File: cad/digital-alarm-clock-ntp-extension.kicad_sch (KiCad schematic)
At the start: 16 parts, among them J1 DigitalClock, J2 Power, J3 M5ATOM Left side, J4 M5ATOM Right side, Q1 2SC1815, Q2 2SC1815, Q3 2SC1815, Q4 2SC1815

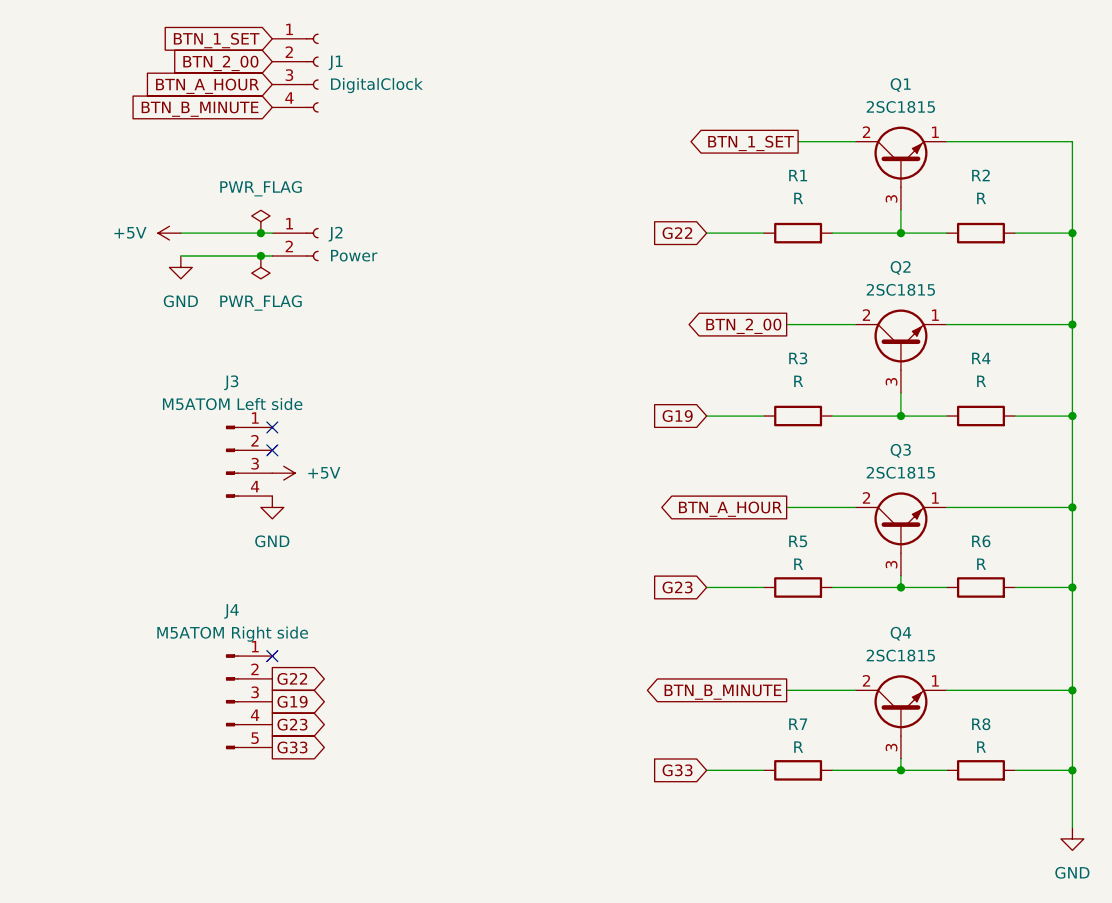
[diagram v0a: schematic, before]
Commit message: feat: 回路図、基板のピンアサインの修正
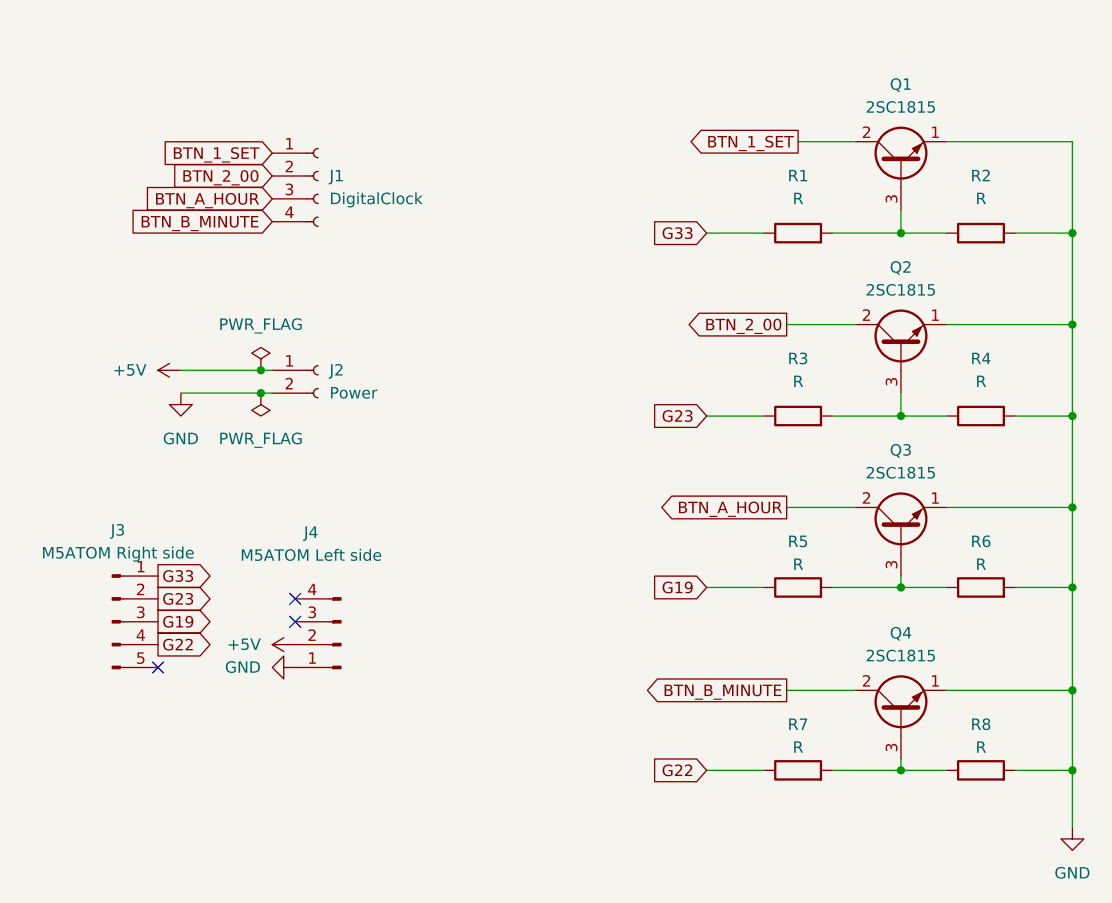
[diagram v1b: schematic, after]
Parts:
- renumbered J4 to J3, J3 to J4
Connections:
- net +5V: now also J4.2 (Pin_2); no longer J4.3 (Pin_3)
- net G19: now also R5.1; no longer R3.1
- net G22: now also J3.4 (Pin_4), R7.1; no longer J3.2 (Pin_2), R1.1
- net G23: now also J3.2 (Pin_2), R3.1; no longer J3.4 (Pin_4), R5.1
- net G33: now also J3.1 (Pin_1), R1.1; no longer J3.5 (Pin_5), R7.1
- net GND: now also J4.1 (Pin_1); no longer J4.4 (Pin_4)
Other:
- moved on the sheet: J1, J2, J3, J4
